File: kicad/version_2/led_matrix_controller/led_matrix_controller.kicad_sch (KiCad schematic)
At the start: 47 parts

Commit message: Fixed led matrix controller
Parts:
- added R5, R6: R, custom_footprint_library:0.4_pitch_resistor, symbol Device:R
- added U4: ~, Package_DIP:DIP-16_W7.62mm, symbol custom_symbol_lib:4bit_adder
- added U5: ~, Package_DIP:DIP-14_W7.62mm, symbol custom_symbol_lib:quad_and
- added U6: ~, Package_DIP:DIP-14_W7.62mm, symbol custom_symbol_lib:6xNOT
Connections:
- net at R2.1, U14.28 (V+), U15.4 (V+)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: now also U5.14 (V+), U6.14 (V+)
- net at U47.9 (4B), U49.1 (0Q), U51.2 (D0)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: no longer U40.1 (IN)
- net at C1.2, D1.1 (K), D2.1 (K)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: now also R5.1, R6.1, U5.10 (4A), U5.12 (3B), U5.13 (3A), U5.7 (GND), U5.9 (4B), U6.1 (I0), U6.11 (I4), U6.3 (I1), U6.5 (I2), U6.7 (GND), U6.9 (I3); no longer U29.8 (2A), U29.9 (2B), U49.11 (1CLK), U49.9 (1D)
- net at U30.3 (I1), U34.3 (OUT), U45.1 (1A)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: now also U5.5 (2B)
- net at U49.12 (1Q#): now also U49.9 (1D), U5.1 (1A)
- net at U49.13 (1Q): now also U40.1 (IN), U5.4 (2A)
- net at U27.5 (Q), U29.1 (0A): now also R5.2
- net at U29.10 (Q2): now also U49.11 (1CLK)
- net at U28.5 (Q), U29.2 (0B): now also R6.2
- net at U17.6 (Q6), U31.7 (D5), U50.8 (Driver_A2): now also U6.13 (I5)
- net at R17.1, U17.7 (Q7), U31.3 (D1): now also U4.5 (A0); no longer U50.9 (Row_A0)
- net at R19.1, U25.1 (Q1), U31.5 (D3): now also U4.14 (A2); no longer U50.11 (Row_A2)
- net at R18.1, U25.15 (Q0), U31.4 (D2): now also U4.3 (A1); no longer U50.10 (Row_A1)
- new net: U5.2 (1B), U6.12 (O5)
- new net: U29.8 (2A), U5.3 (1Q)
- new net: U29.9 (2B), U5.6 (2Q)
- new net: U4.1 (Σ1), U50.10 (Row_A1)
- new net: U4.11 (B3), U4.15 (B2), U4.16 (V+), U4.2 (B1), U4.6 (B0)
- new net: U4.12 (A3), U4.7 (C_IN), U4.8 (GND)
- new net: U4.13 (Σ2), U50.11 (Row_A2)
- new net: U4.4 (Σ0), U50.9 (Row_A0)
- no-connect marks 27 -> 33
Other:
- note added: "Bit address rollover seguence start"
- note added: "Driver address rollover sequence"
- note added: "LE control latch CLK"
- note added: "Subtract 1"

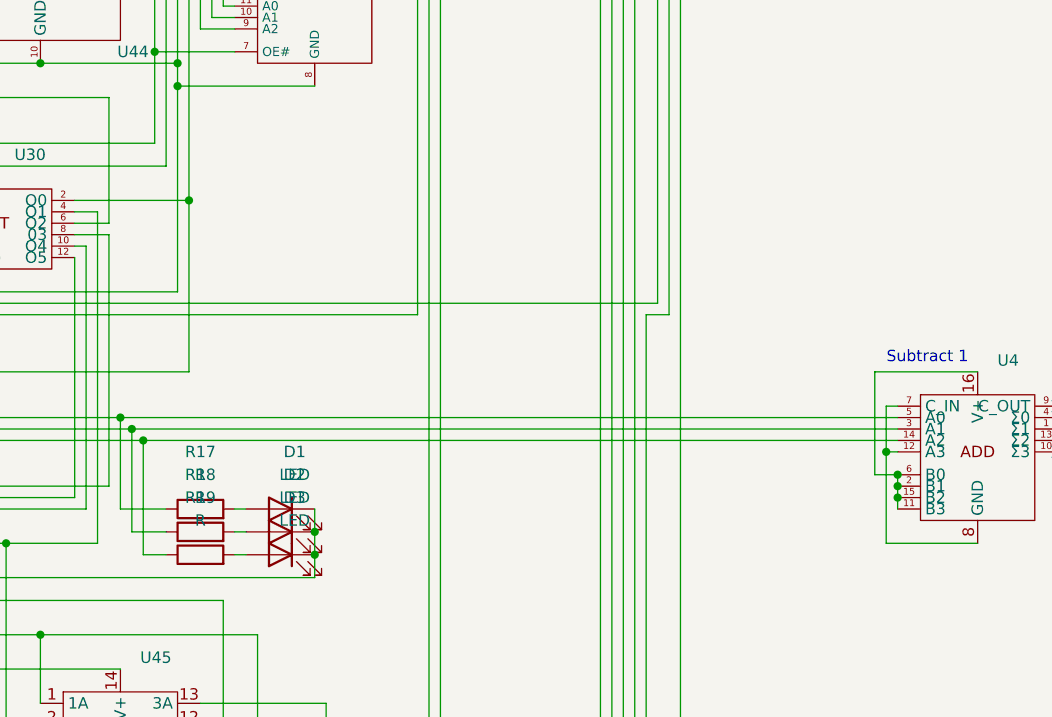
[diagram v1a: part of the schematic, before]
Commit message: Tetris program draw-shape and init-next-shape-from-storage functions work
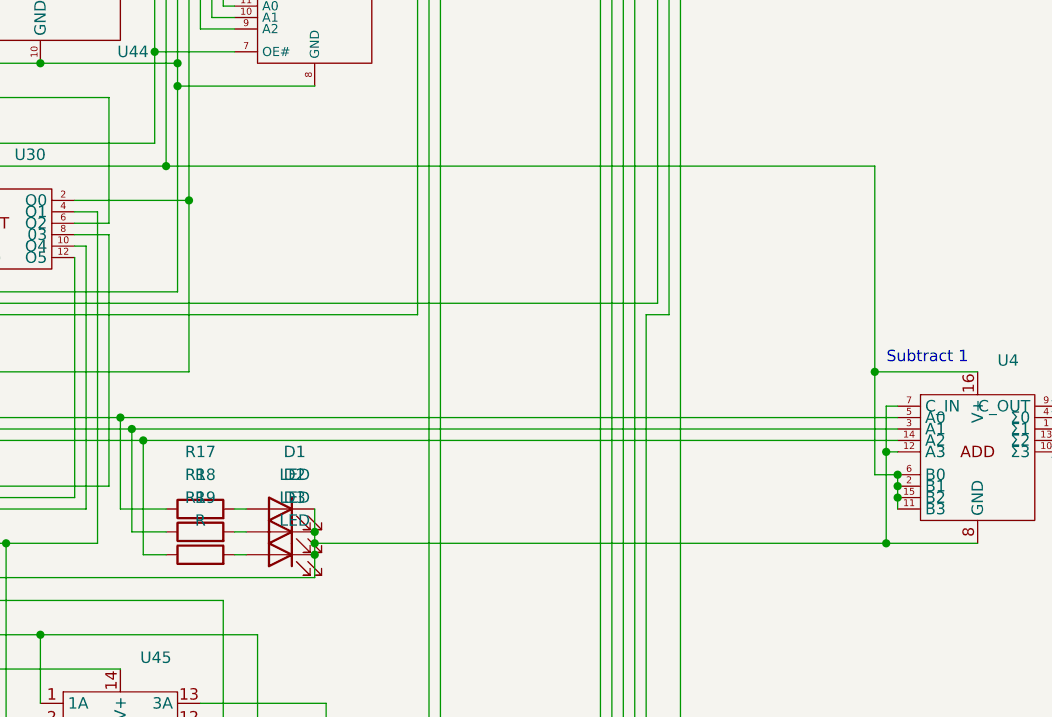
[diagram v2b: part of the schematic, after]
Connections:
- net at R2.1, U14.28 (V+), U15.4 (V+)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: now also U4.11 (B3), U4.15 (B2), U4.16 (V+), U4.2 (B1), U4.6 (B0)
- net at C1.2, D1.1 (K), D2.1 (K)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: now also U4.12 (A3), U4.7 (C_IN), U4.8 (GND)
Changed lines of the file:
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@@
 	)
 	(junction
+		(at 472.44 200.66)
+		(diameter 0)
+		(color 0 0 0 0)
+	)
+	(junction
 		(at 535.94 190.5)
 		(diameter 0)
@@
 	)
 	(junction
+		(at 534.67 181.61)
+		(diameter 0)
+		(color 0 0 0 0)
+	)
+	(junction
 		(at 353.06 72.39)
 		(diameter 0)
@@
 	)
 	(junction
+		(at 535.94 200.66)
+		(diameter 0)
+		(color 0 0 0 0)
+	)
+	(junction
 		(at 501.65 113.03)
 		(diameter 0)
@@
 	)
 	(junction
+		(at 455.93 158.75)
+		(diameter 0)
+		(color 0 0 0 0)
+	)
+	(junction
 		(at 455.93 99.06)
 		(diameter 0)
@@
 	(wire
 		(pts
-			(xy 472.44 199.39) (xy 472.44 201.93)
+			(xy 472.44 199.39) (xy 472.44 200.66)
 		)
 		(stroke
@@
 	(wire
 		(pts
+			(xy 472.44 200.66) (xy 472.44 201.93)
+		)
+		(stroke
+			(width 0)
+			(type default)
+		)
+	)
+	(wire
+		(pts
 			(xy 349.25 101.6) (xy 304.8 101.6)
 		)
@@
 	(wire
 		(pts
+			(xy 472.44 200.66) (xy 535.94 200.66)
+		)
+		(stroke
+			(width 0)
+			(type default)
+		)
+	)
+	(wire
+		(pts
 			(xy 355.6 64.77) (xy 567.69 64.77)
 		)
@@
 	(wire
 		(pts
+			(xy 534.67 158.75) (xy 534.67 181.61)
+		)
+		(stroke
+			(width 0)
+			(type default)
+		)
+	)
+	(wire
+		(pts
 			(xy 334.01 298.45) (xy 334.01 313.69)
 		)
@@
 		)
 		(stroke
+			(width 0)
+			(type default)
+		)
+	)
+	(wire
+		(pts
+			(xy 455.93 158.75) (xy 534.67 158.75)
+		)
+		(stroke

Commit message: Brushless controller
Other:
- note added: "It works when test LED is connected here"
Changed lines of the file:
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@@
 		)
 	)
+	(polyline
+		(pts
+			(xy 492.76 102.87) (xy 494.03 101.6)
+		)
+		(stroke
+			(width 0)
+			(type default)
+		)
+	)
 	(wire
 		(pts
@@
 		)
 	)
+	(polyline
+		(pts
+			(xy 494.03 92.71) (xy 494.03 101.6)
+		)
+		(stroke
+			(width 0)
+			(type default)
+		)
+	)
 	(wire
 		(pts
@@
 	(text "Control latch CLK"
 		(exclude_from_sim no)
-		(at 522.986 103.124 0)
+		(at 522.732 102.87 0)
 		(effects
 			(font
@@
 		(effects
 			(font
+				(size 1.27 1.27)
+			)
+		)
+	)
+	(text "It works when test LED is connected here"
+		(exclude_from_sim no)
+		(at 514.604 92.71 0)
+		(effects
+			(font

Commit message: Point test and work on optimizing tetris
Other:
- note added: "Control latch CLK (DELAY W/ CAP)"
- note added: "LE control latch CLK (DELAY W/ CAP)"
- note removed: "Control latch CLK"
- note removed: "LE control latch CLK"
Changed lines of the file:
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@@
 		)
 	)
-	(text "Control latch CLK"
+	(text "Control latch CLK (DELAY W/ CAP)"
 		(exclude_from_sim no)
-		(at 522.732 102.87 0)
+		(at 514.35 102.87 0)
 		(effects
 			(font
 				(size 1.27 1.27)
 			)
+			(justify left)
 		)
 	)
@@
 		)
 	)
-	(text "LE control latch CLK"
+	(text "LE control latch CLK (DELAY W/ CAP)"
 		(exclude_from_sim no)
-		(at 524.51 105.664 0)
+		(at 514.604 105.664 0)
 		(effects
 			(font
 				(size 1.27 1.27)
 			)
+			(justify left)
 		)
 	)
